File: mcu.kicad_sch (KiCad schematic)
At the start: 42 parts, among them J2 Conn_01x10, J4 Micro_SD_Card_Det1, J6 Conn_01x03_Pin, J7 RFShield_TwoPieces, SW1 SW_Push, SW2 SW_Push, SW3 SW_Push, SW4 SW_Push, U1 nRF54L15-QFXX, U9 TPD6F003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

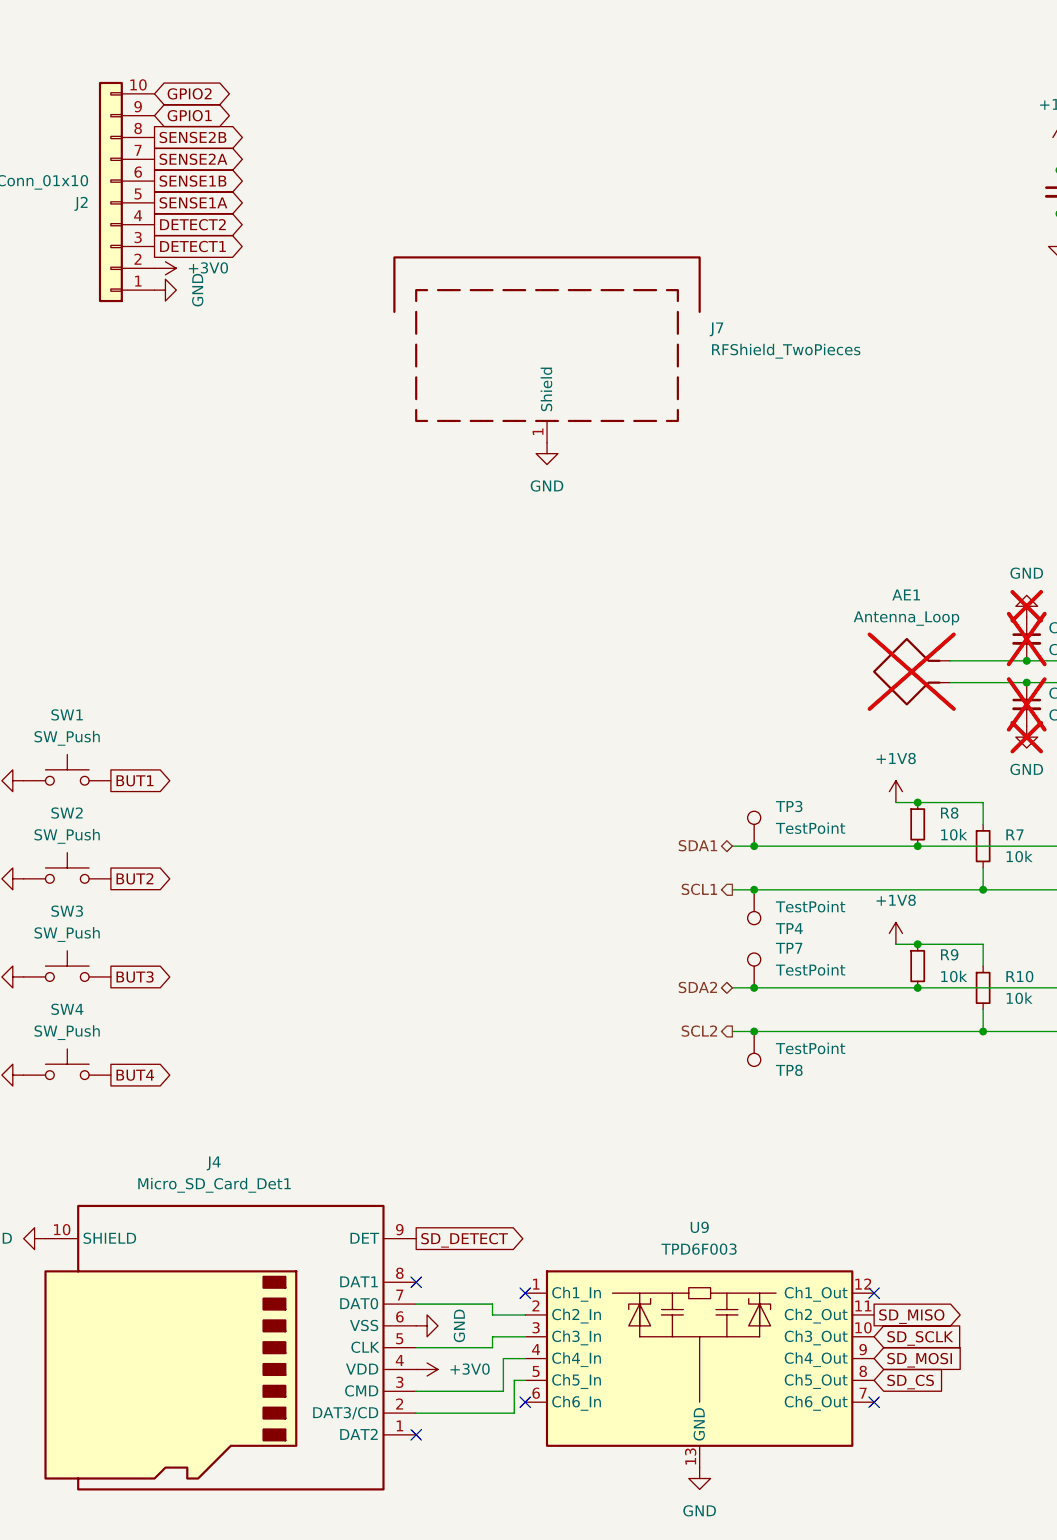
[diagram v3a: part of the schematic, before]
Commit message: add TVS diodes on I/O port
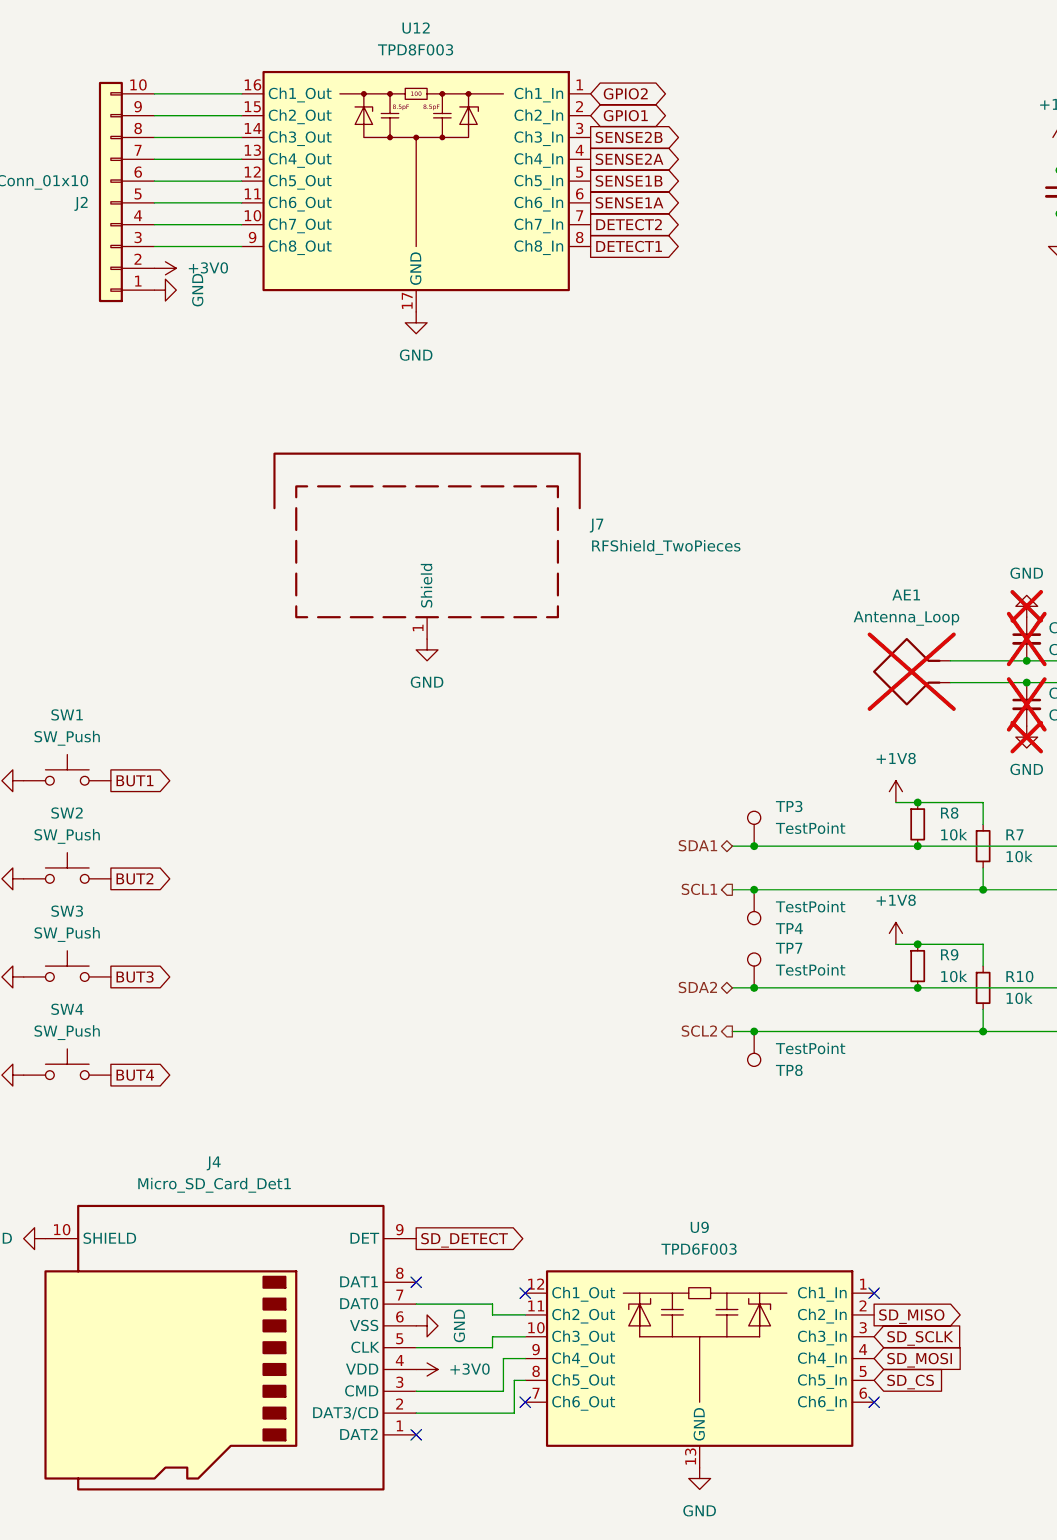
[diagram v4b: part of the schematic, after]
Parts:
- added U12: TPD8F003, Package_SON:WSON-16_3.3x1.35_P0.4mm, symbol Power_Protection:TPD8F003
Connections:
- net DETECT1: now also U12.8 (Ch8_In); no longer J2.3 (Pin_3)
- net DETECT2: now also U12.7 (Ch7_In); no longer J2.4 (Pin_4)
- net GND: now also U12.17 (GND)
- net GPIO1: now also U12.2 (Ch2_In); no longer J2.9 (Pin_9)
- net GPIO2: now also U12.1 (Ch1_In); no longer J2.10 (Pin_10)
- net SD_CS: now also U9.5 (Ch5_In); no longer U9.8 (Ch5_Out)
- net SD_MISO: now also U9.2 (Ch2_In); no longer U9.11 (Ch2_Out)
- net SD_MOSI: now also U9.4 (Ch4_In); no longer U9.9 (Ch4_Out)
- net SD_SCLK: now also U9.3 (Ch3_In); no longer U9.10 (Ch3_Out)
- net SENSE1A: now also U12.6 (Ch6_In); no longer J2.5 (Pin_5)
- net SENSE1B: now also U12.5 (Ch5_In); no longer J2.6 (Pin_6)
- net SENSE2A: now also U12.4 (Ch4_In); no longer J2.7 (Pin_7)
- net SENSE2B: now also U12.3 (Ch3_In); no longer J2.8 (Pin_8)
- net at J4.7 (DAT0): now also U9.11 (Ch2_Out); no longer U9.2 (Ch2_In)
- net at J4.5 (CLK): now also U9.10 (Ch3_Out); no longer U9.3 (Ch3_In)
- net at J4.3 (CMD): now also U9.9 (Ch4_Out); no longer U9.4 (Ch4_In)
- net at J4.2 (DAT3/CD): now also U9.8 (Ch5_Out); no longer U9.5 (Ch5_In)
- new net: J2.4 (Pin_4), U12.10 (Ch7_Out)
- new net: J2.5 (Pin_5), U12.11 (Ch6_Out)
- new net: J2.6 (Pin_6), U12.12 (Ch5_Out)
- new net: J2.7 (Pin_7), U12.13 (Ch4_Out)
- new net: J2.8 (Pin_8), U12.14 (Ch3_Out)
- new net: J2.9 (Pin_9), U12.15 (Ch2_Out)
- new net: J2.10 (Pin_10), U12.16 (Ch1_Out)
- new net: J2.3 (Pin_3), U12.9 (Ch8_Out)
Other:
- moved on the sheet: J7
